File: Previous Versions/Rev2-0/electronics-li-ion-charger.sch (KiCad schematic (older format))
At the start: 17 parts, among them J1 Conn_01x01_Male, J2 Conn_01x01_Male, J3 USB_B_Micro, J4 Conn_01x03_Male, U1 MCP73831-2-OT

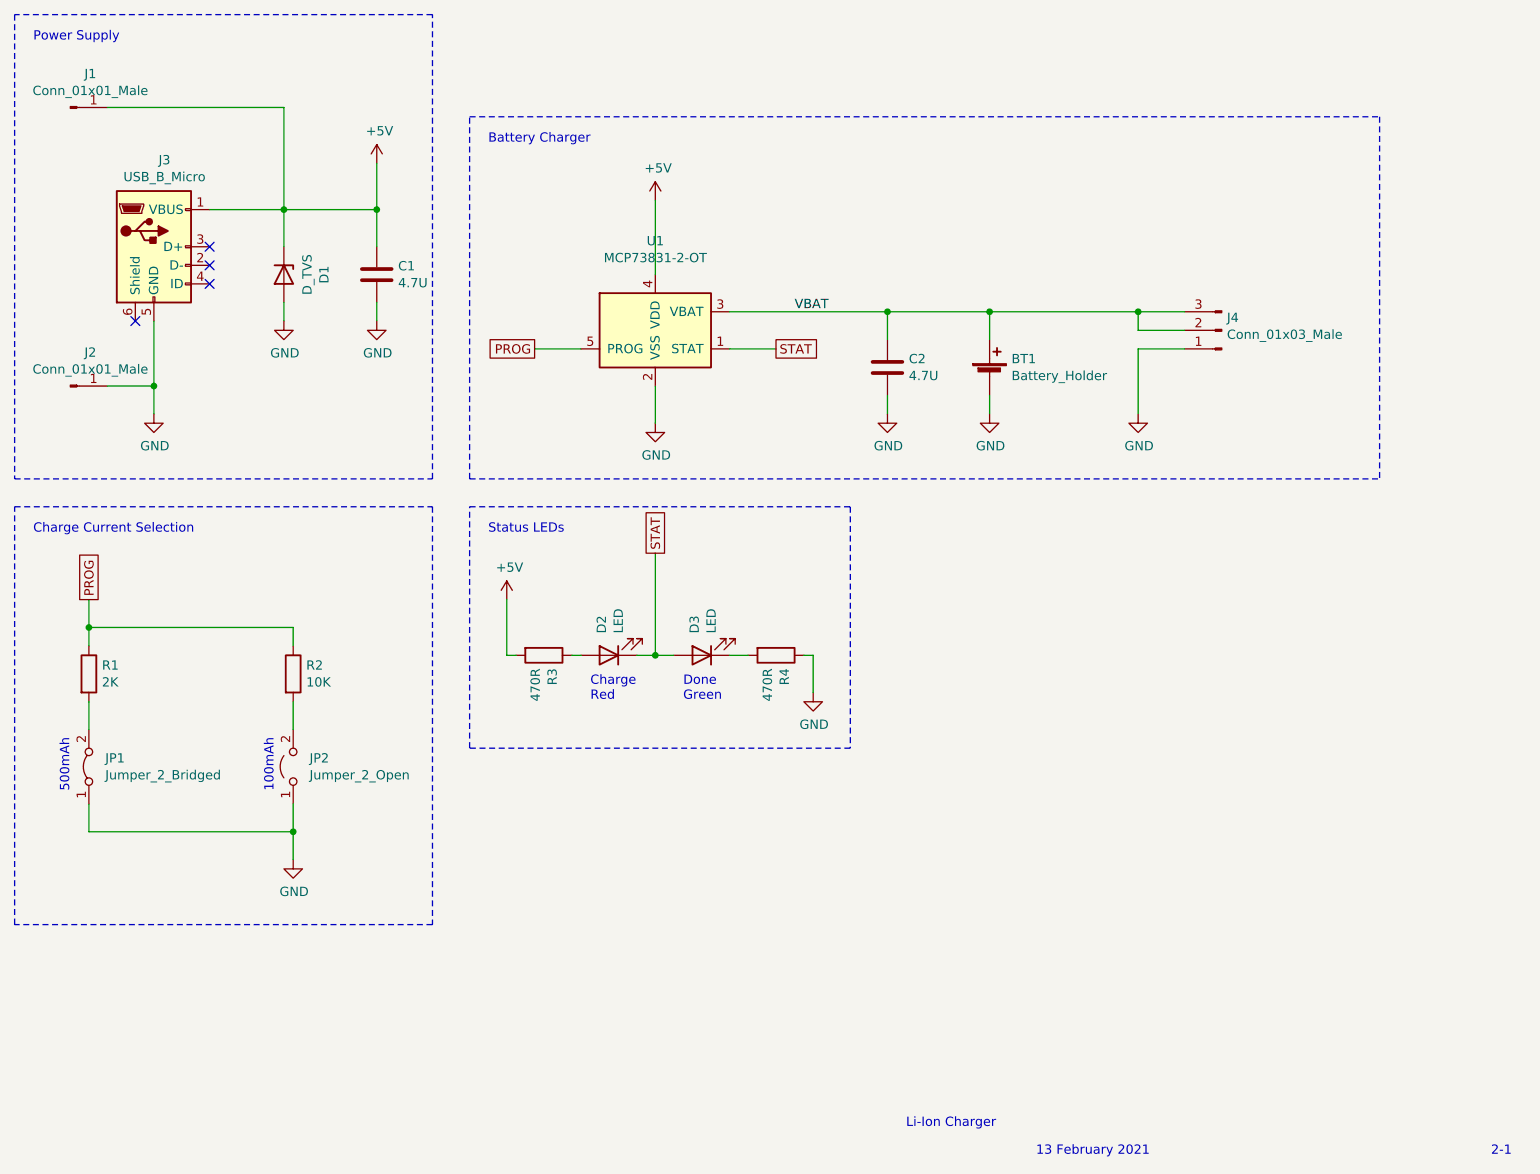
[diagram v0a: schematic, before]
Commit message: Rev2-1: Fix LED short circuit and PROG trace.
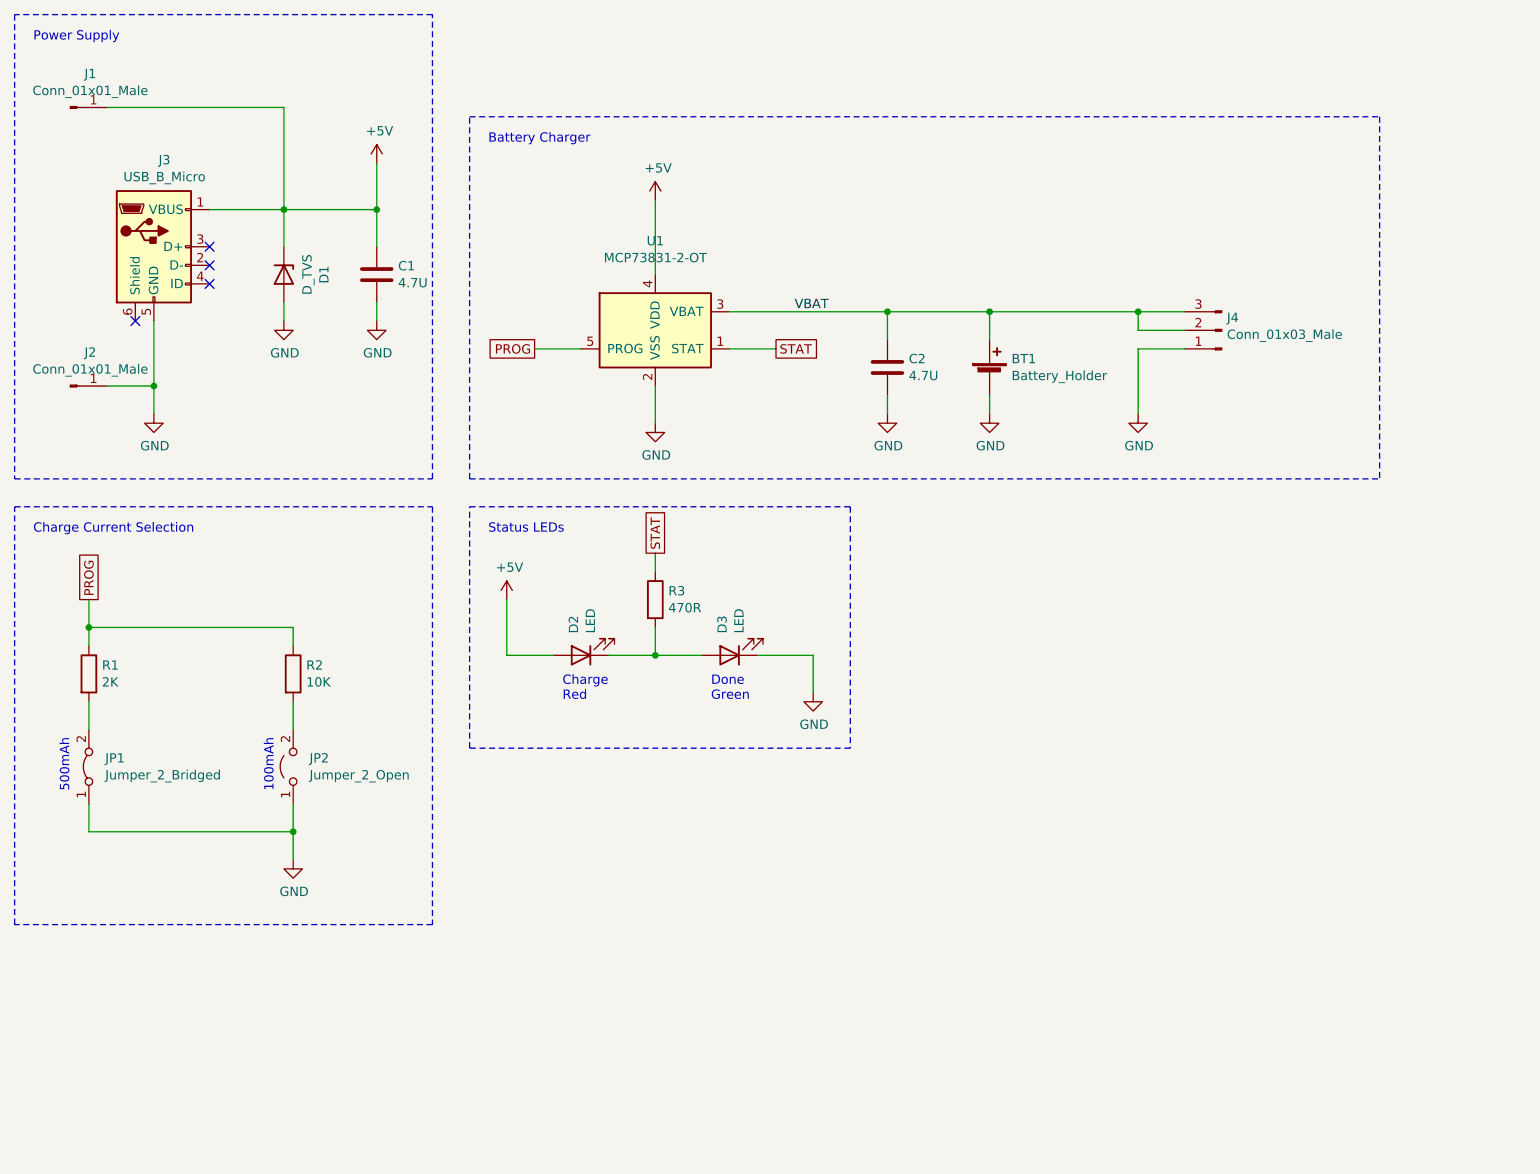
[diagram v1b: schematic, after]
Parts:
- removed R4: 470R, Resistor_SMD:R_1206_3216Metric_Pad1.30x1.75mm_HandSolder, symbol Device:R
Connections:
- net +5V: now also D2.2 (A); no longer R3.2
- net GND: now also D3.1 (K)
- net STAT: now also R3.1; no longer D2.1 (K), D3.2 (A)
- new net: D2.1 (K), D3.2 (A), R3.2
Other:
- note removed: "13 February 2021"
- note removed: "2-1"
- note removed: "Li-Ion Charger"
- moved on the sheet: D2, D3, R3
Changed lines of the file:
@@
 L Device:R R3
 U 1 1 5FFB5567
-P 5500 4950
-F 0 "R3" H 5570 4996 50  0000 L CNN
-F 1 "470R" H 5570 4905 50  0000 L CNN
-F 2 "Resistor_SMD:R_1206_3216Metric_Pad1.30x1.75mm_HandSolder" V 5430 4950 50  0001 C CNN
-F 3 "~" H 5500 4950 50  0001 C CNN
-	1    5500 4950
-	0    1    1    0
+P 6100 4650
+F 0 "R3" H 6170 4696 50  0000 L CNN
+F 1 "470R" H 6170 4605 50  0000 L CNN
+F 2 "Resistor_SMD:R_1206_3216Metric_Pad1.30x1.75mm_HandSolder" V 6030 4650 50  0001 C CNN
+F 3 "~" H 6100 4650 50  0001 C CNN
+	1    6100 4650
+	1    0    0    -1
 $EndComp
 $Comp
@@
 L Device:LED D3
 U 1 1 5FFB6F7B
-P 6350 4950
-F 0 "D3" V 6389 4832 50  0000 R CNN
-F 1 "LED" V 6298 4832 50  0000 R CNN
-F 2 "LED_SMD:LED_1206_3216Metric_Pad1.42x1.75mm_HandSolder" H 6350 4950 50  0001 C CNN
-F 3 "~" H 6350 4950 50  0001 C CNN
-	1    6350 4950
+P 6500 4950
+F 0 "D3" V 6539 4832 50  0000 R CNN
+F 1 "LED" V 6448 4832 50  0000 R CNN
+F 2 "LED_SMD:LED_1206_3216Metric_Pad1.42x1.75mm_HandSolder" H 6500 4950 50  0001 C CNN
+F 3 "~" H 6500 4950 50  0001 C CNN
+	1    6500 4950
 	-1   0    0    1
 $EndComp
@@
 L Device:LED D2
 U 1 1 5FFB7C3E
-P 5850 4950
-F 0 "D2" V 5889 4832 50  0000 R CNN
-F 1 "LED" V 5798 4832 50  0000 R CNN
-F 2 "LED_SMD:LED_1206_3216Metric_Pad1.42x1.75mm_HandSolder" H 5850 4950 50  0001 C CNN
-F 3 "~" H 5850 4950 50  0001 C CNN
-	1    5850 4950
+P 5700 4950
+F 0 "D2" V 5739 4832 50  0000 R CNN
+F 1 "LED" V 5648 4832 50  0000 R CNN
+F 2 "LED_SMD:LED_1206_3216Metric_Pad1.42x1.75mm_HandSolder" H 5700 4950 50  0001 C CNN
+F 3 "~" H 5700 4950 50  0001 C CNN
+	1    5700 4950
 	-1   0    0    1
 $EndComp
@@
 	6500 3300 6750 3300
 Wire Wire Line
-	6000 4950 6100 4950
+	6100 4400 6100 4500
+Wire Wire Line
+	5850 4950 6100 4950
 Connection ~ 6100 4950
 Text Notes 2950 5400 3    50   ~ 0
@@
 Text Notes 5200 4300 0    50   ~ 0
 Status LEDs
-Text Notes 5750 5200 0    50   ~ 0
+Text Notes 5600 5200 0    50   ~ 0
 Charge\nRed
-Text Notes 6250 5200 0    50   ~ 0
+Text Notes 6400 5200 0    50   ~ 0
 Done\nGreen
 Wire Notes Line
@@
 	5100 4000 10000 4000
 Wire Wire Line
-	6100 4950 6200 4950
+	6100 4800 6100 4950
+Wire Wire Line
+	6100 4950 6350 4950
 $Comp
 L power:GND #PWR0105
@@
 	5300 4650 5300 4950
 Wire Wire Line
-	5300 4950 5350 4950
-Wire Wire Line
-	6500 4950 6600 4950
+	5300 4950 5550 4950
+Wire Wire Line
+	6650 4950 6950 4950
 Wire Wire Line
 	6950 4950 6950 5150
@@
 Wire Notes Line
 	7150 5450 5100 5450
-Text Notes 8150 7650 0    50   ~ 0
-13 February 2021
-Text Notes 10600 7650 0    50   ~ 0
-2-1
-$Comp
-L Device:R R4
-U 1 1 60284F6E
-P 6750 4950
-F 0 "R4" H 6820 4996 50  0000 L CNN
-F 1 "470R" H 6820 4905 50  0000 L CNN
-F 2 "Resistor_SMD:R_1206_3216Metric_Pad1.30x1.75mm_HandSolder" V 6680 4950 50  0001 C CNN
-F 3 "~" H 6750 4950 50  0001 C CNN
-	1    6750 4950
-	0    1    1    0
-$EndComp
-Wire Wire Line
-	6100 4400 6100 4950
-Wire Wire Line
-	5650 4950 5700 4950
-Wire Wire Line
-	6900 4950 6950 4950
-Text Notes 7450 7500 0    50   ~ 0
-Li-Ion Charger
 $EndSCHEMATC
